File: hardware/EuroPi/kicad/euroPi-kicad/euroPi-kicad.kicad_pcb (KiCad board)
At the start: 2 copper layers, 134.1 x 128.9 mm, 95 parts, among them J1 Output 1 Jack, J10 Eurorack Power 2x8 16p, J11 Conn_01x13_Socket, J12 OLED 64x128, J13 USB_B_Micro, J14 Conn_01x03_Pin, J16 Conn_02x04_Top_Bottom, J17 Conn_01x13_Pin, J18 Conn_01x04_Pin, J19 Conn_01x04_Socket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

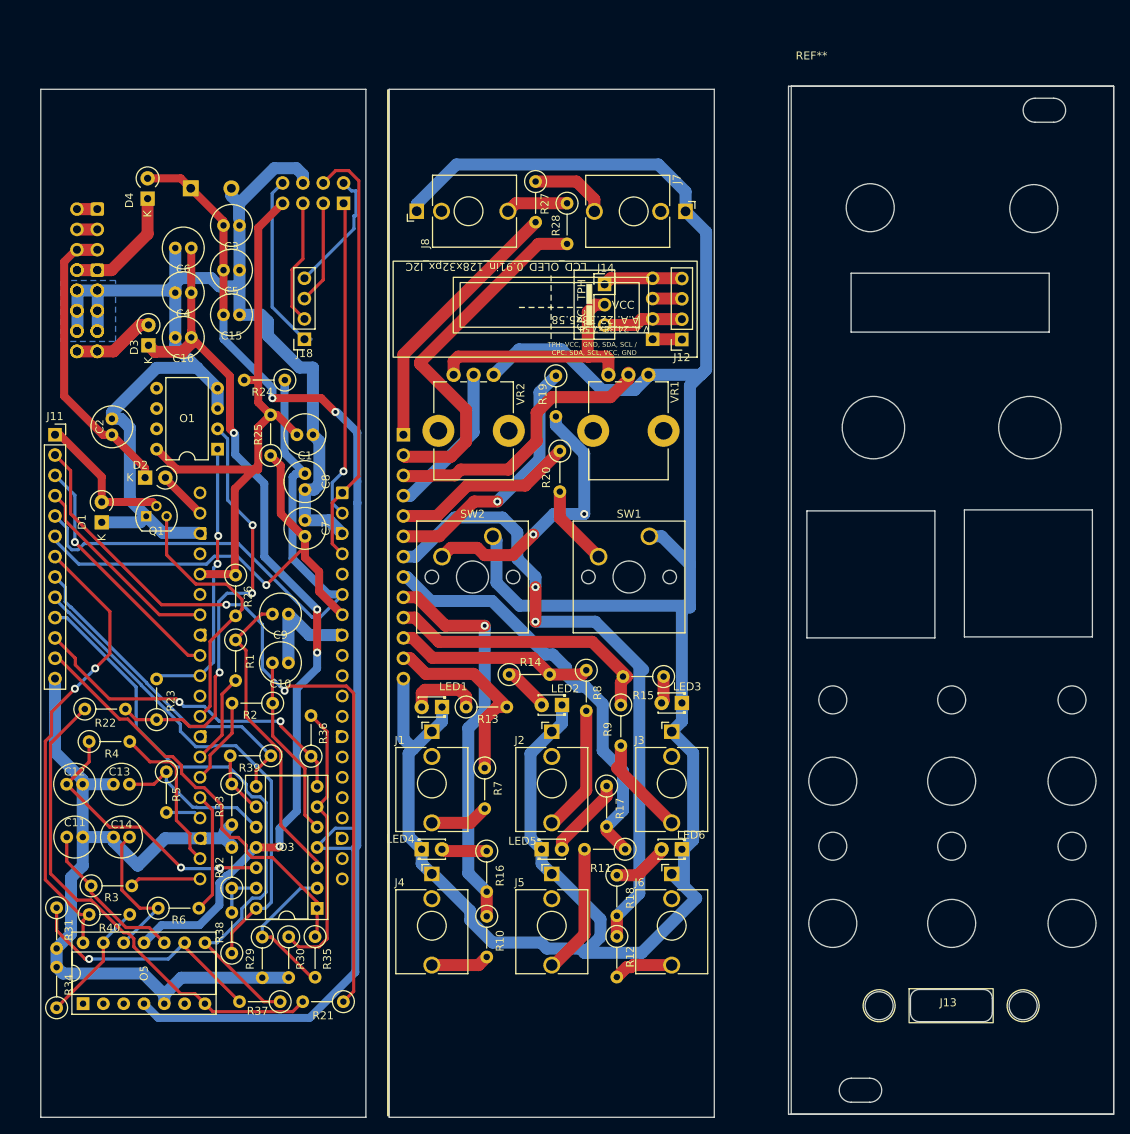
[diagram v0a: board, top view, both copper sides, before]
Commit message: cleaning pcb fixing connector i2c
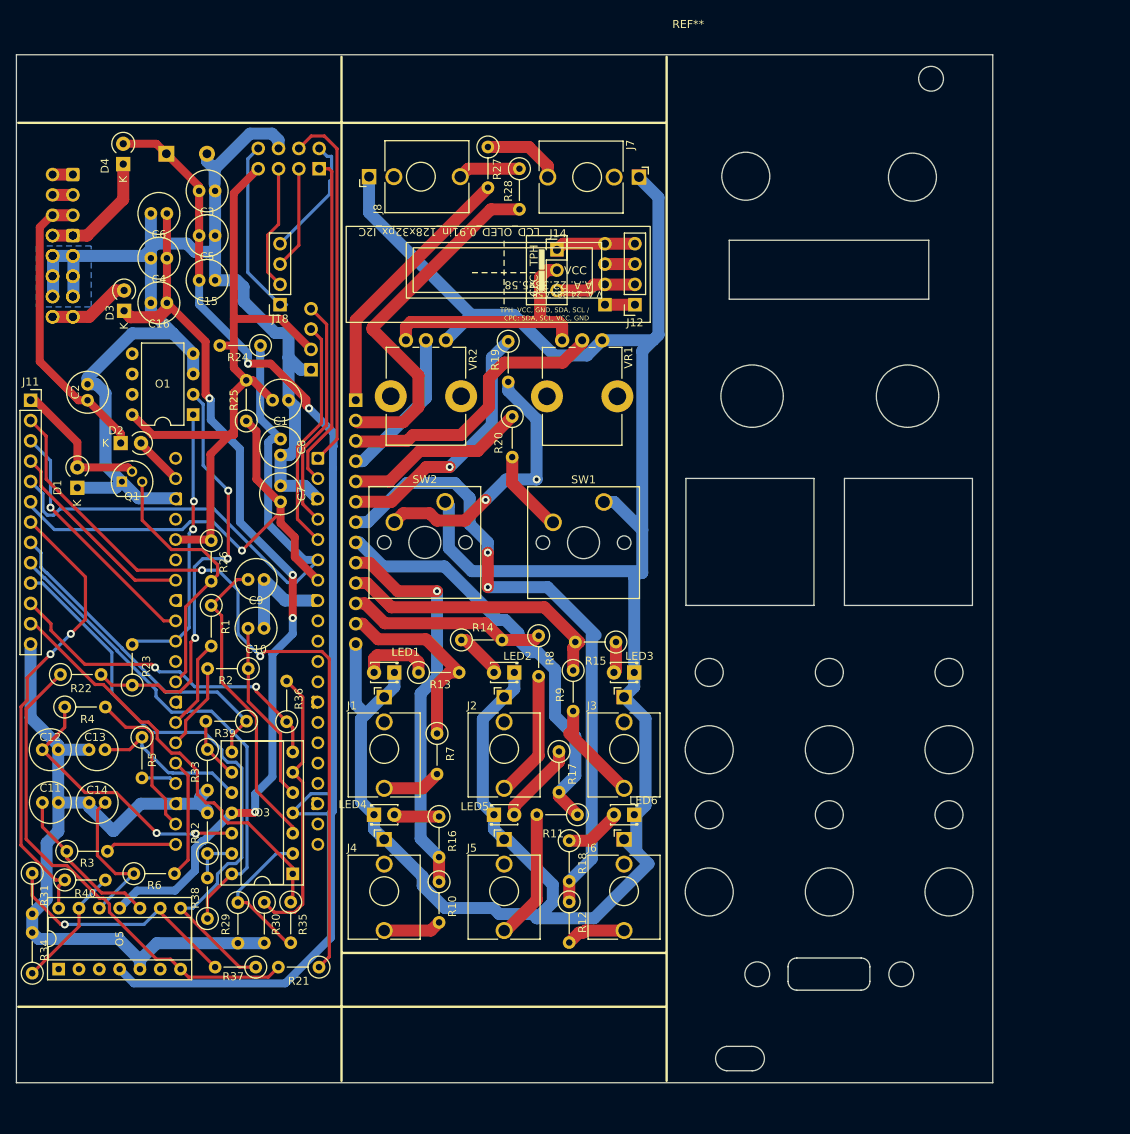
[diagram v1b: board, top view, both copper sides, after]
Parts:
- added J15: Conn_01x04_Pin, Connector_PinSocket_2.54mm:PinSocket_1x04_P2.54mm_Vertical, B.Cu at (77.5, 64.8)
- J13: moved to B.Cu
- moved REF** 15.9 mm to (122.1, 25.4)
- moved J13 15.7 mm to (142.2, 140.3), turned to 180 degrees
- moved R10 7.36 mm to (93.5, 128.8)
- moved R12 7.36 mm to (109.7, 131.3)
- moved R17 7.36 mm to (108.5, 112.5)
- moved R20 7.36 mm to (102.6, 70.6)
- moved R9 7.36 mm to (110.2, 102.4)
- moved R27 7.36 mm to (99.6, 36.9)
- moved J1 7.36 mm to (86.6, 105.7)
- moved J14 7.36 mm to (108.2, 49.8)
- moved J19 7.36 mm to (114.2, 56.6)
- moved J2 7.36 mm to (101.6, 105.7)
- moved J3 7.36 mm to (116.6, 105.7)
- moved J4 7.36 mm to (86.6, 123.5)
- moved J5 7.36 mm to (101.6, 123.5)
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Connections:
- J16 pad 1: CPC_SCL -> GP1
- J16 pad 6: CPC_SDA -> GP0
- U2 pad 1: CPC_SDA -> GP0
- U2 pad 2: CPC_SCL -> GP1
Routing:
- net GP0: track 0.00 -> 45.8 mm
- net GP1: track 0.00 -> 41.9 mm
- net CPC_SDA: track 54.1 -> 29.1 mm
- net CPC_GND: track 589.9 -> 574.6 mm
- net CPC_VCC: track 106.3 -> 117.6 mm
- net CPC_SCL: track 40.0 -> 29.1 mm, vias 1 -> 0
- net ~: track 156.8 -> 155.2 mm
- net Net-(LED3-A): track 3.41 -> 3.91 mm
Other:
- board size 134.1 x 128.9 mm -> 122 x 128.5 mm
- board text added: "NOTE : 1. edge cut inner radius 1.0mm / 60mil unless otherwise already defined."

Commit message: fixed eurorack connector to correct pin1 imported graphics
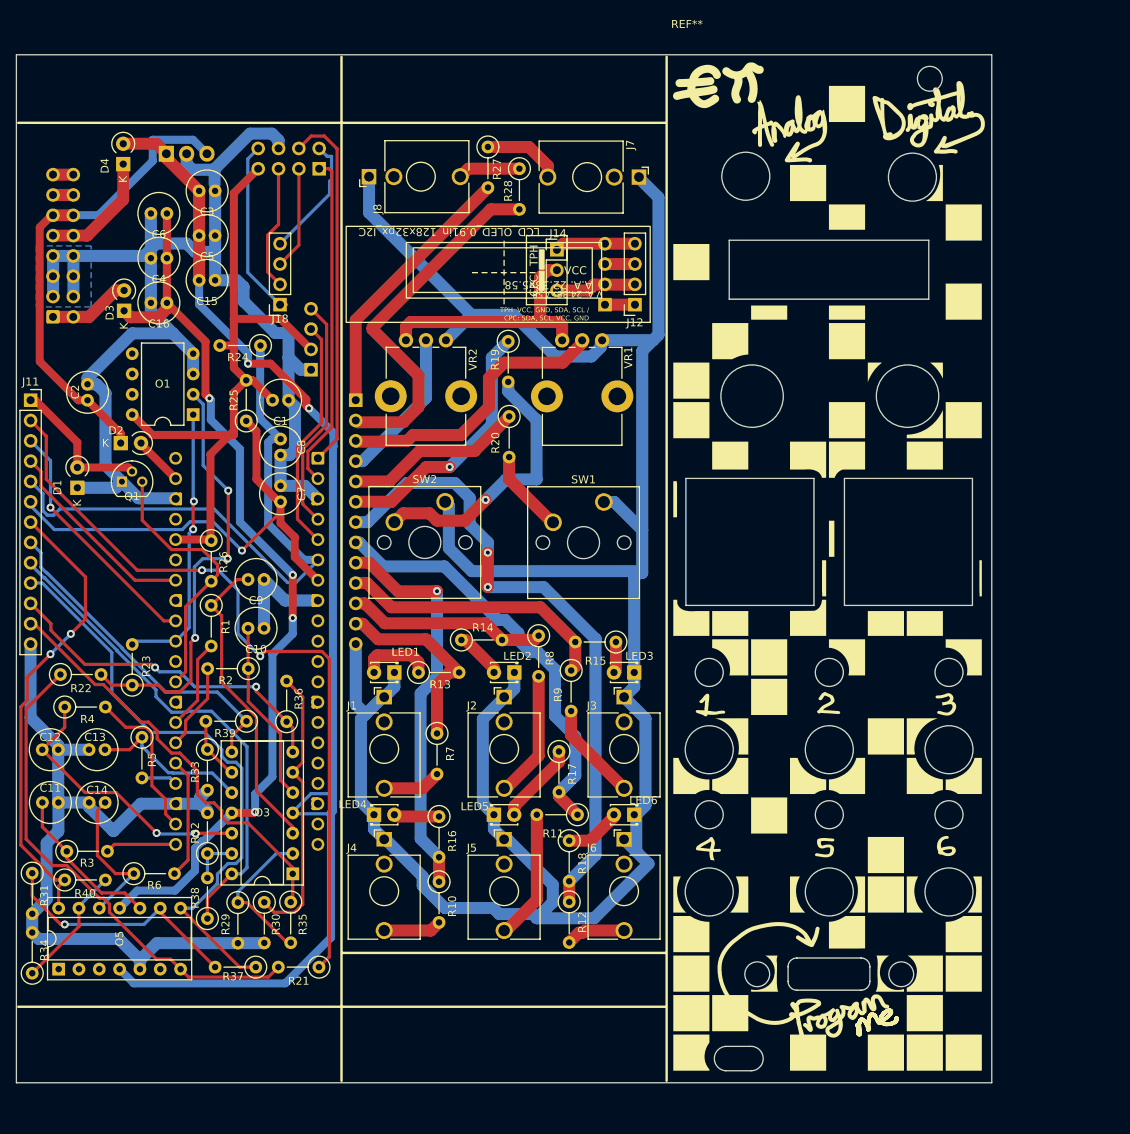
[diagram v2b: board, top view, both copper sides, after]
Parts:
- removed J9: Eurorack Power 2x5 10p, Connector_IDC:IDC-Header_2x05_P2.54mm_Vertical
- J10: footprint Connector_IDC:IDC-Header_2x08_P2.54mm_Vertical -> Library:IDC-Header_euroRack-2x08_and_2x05_P2.54mm_Vertical
- U1: footprint Package_TO_SOT_THT:TO-220-2_Vertical -> Package_TO_SOT_THT:TO-220-3_Vertical
- moved J10 18.0 mm to (45.2, 58.2), turned to 0 degrees
- moved R20 0.38 mm to (102.2, 70.6)
- moved R9 0.25 mm to (110.0, 102.4)
- moved REF** 0.15 mm to (121.9, 25.4)
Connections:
- net CPC_SCL renamed GP3
- net CPC_SDA renamed GP2
- net CPC_VCC renamed I2C_VCC
- C1 pad 2: CPC_GND -> I2C_GND
- C10 pad 2: CPC_GND -> I2C_GND
- C11 pad 2: CPC_GND -> I2C_GND
- C12 pad 2: CPC_GND -> I2C_GND
- C13 pad 2: CPC_GND -> I2C_GND
- C14 pad 2: CPC_GND -> I2C_GND
- C15 pad 2: CPC_GND -> I2C_GND
- C16 pad 1: CPC_GND -> I2C_GND
- C2 pad 2: CPC_GND -> I2C_GND
- C3 pad 2: CPC_GND -> I2C_GND
- C4 pad 1: CPC_GND -> I2C_GND
- C5 pad 2: CPC_GND -> I2C_GND
- C6 pad 1: CPC_GND -> I2C_GND
- C7 pad 2: CPC_GND -> I2C_GND
- C8 pad 2: CPC_GND -> I2C_GND
- C9 pad 2: CPC_GND -> I2C_GND
- D1 pad 1: CPC_GND -> I2C_GND
- J1 pad S: CPC_GND -> I2C_GND
- J10 pad 1: Net-(J10-Pin_1) -> Net-(D3-K)
- J10 pad 10: CPC_GND -> Net-(D4-A)
- J10 pad 11: CPC_GND -> +5V
- J10 pad 12: CPC_GND -> +5V
- J10 pad 13: CPC_GND -> Net-(J10-Pin_13)
- J10 pad 14: CPC_GND -> Net-(J10-Pin_13)
- J10 pad 15: Net-(D3-K) -> Net-(J10-Pin_15)
- J10 pad 16: Net-(D3-K) -> Net-(J10-Pin_15)
- J10 pad 2: Net-(J10-Pin_1) -> Net-(D3-K)
- J10 pad 3: Net-(J10-Pin_3) -> I2C_GND
- J10 pad 4: Net-(J10-Pin_3) -> I2C_GND
- J10 pad 5: +5V -> I2C_GND
- J10 pad 6: +5V -> I2C_GND
- J10 pad 7: Net-(D4-A) -> I2C_GND
- J10 pad 8: Net-(D4-A) -> I2C_GND
- J10 pad 9: CPC_GND -> Net-(D4-A)
- J11 pad 13: CPC_GND -> I2C_GND
- J15 pad 1: CPC_GND -> I2C_GND
- J16 pad 7: CPC_GND -> I2C_GND
- J17 pad 13: CPC_GND -> I2C_GND
- J2 pad S: CPC_GND -> I2C_GND
- J3 pad S: CPC_GND -> I2C_GND
- J4 pad S: CPC_GND -> I2C_GND
- J5 pad S: CPC_GND -> I2C_GND
- J6 pad S: CPC_GND -> I2C_GND
- J7 pad S: CPC_GND -> I2C_GND
- J8 pad S: CPC_GND -> I2C_GND
- LED1 pad 1: CPC_GND -> I2C_GND
- LED2 pad 1: CPC_GND -> I2C_GND
- LED3 pad 1: CPC_GND -> I2C_GND
- LED4 pad 1: CPC_GND -> I2C_GND
- LED5 pad 1: CPC_GND -> I2C_GND
- LED6 pad 1: CPC_GND -> I2C_GND
- O1 pad 3: CPC_GND -> I2C_GND
- O1 pad 4: CPC_GND -> I2C_GND
- O5 pad 5: CPC_GND -> I2C_GND
- Q1 pad 1: CPC_GND -> I2C_GND
- R29 pad 2: CPC_GND -> I2C_GND
- R30 pad 2: CPC_GND -> I2C_GND
- R31 pad 2: CPC_GND -> I2C_GND
- R32 pad 2: CPC_GND -> I2C_GND
- R33 pad 2: CPC_GND -> I2C_GND
- R34 pad 2: CPC_GND -> I2C_GND
- SW1 pad 1: CPC_GND -> I2C_GND
- SW2 pad 1: CPC_GND -> I2C_GND
- U1 pad 2: CPC_GND -> I2C_GND
- U2 pad 13: CPC_GND -> I2C_GND
- U2 pad 18: CPC_GND -> I2C_GND
- U2 pad 23: CPC_GND -> I2C_GND
- U2 pad 28: CPC_GND -> I2C_GND
- U2 pad 3: CPC_GND -> I2C_GND
- U2 pad 33: CPC_GND -> I2C_GND
- U2 pad 38: CPC_GND -> I2C_GND
- U2 pad 8: CPC_GND -> I2C_GND
- VR1 pad 3: CPC_GND -> I2C_GND
- VR2 pad 3: CPC_GND -> I2C_GND
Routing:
- net I2C_GND: track 0.00 -> 577.9 mm
- net CPC_GND: track 574.6 -> 0.00 mm
- net +5V: track 36.7 -> 59.7 mm
- net Net-(J10-Pin_3): track 2.54 -> 0.00 mm
- net Net-(J10-Pin_15): track 0.00 -> 2.54 mm
- net Net-(J10-Pin_13): track 0.00 -> 2.54 mm
- net Net-(J10-Pin_1): track 2.54 -> 0.00 mm
- net CJ3: track 108.9 -> 108.3 mm
- net Net-(R19-Pad2): vias 2 -> 1
- added copper zone on B.Cu, net I2C_GND
- removed copper zone on B.Cu, net CPC_GND
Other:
- board size 122 x 128.5 mm -> 121.9 x 128.5 mm
